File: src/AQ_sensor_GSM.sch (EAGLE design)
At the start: 83 parts, among them IC2 MCP73831/OT, J1 F-1X03-SIP-100-32, SW1 PCM12SMTR, U2 TEXAS_INSTRUMENTS_SN74HC125TE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, U3 TEXAS_INSTRUMENTS_LM1117IMP-3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, U4 ESP8266-12E/ESP-12E, U5 TP4056, U6 CP2102N-A02-GQFN28, U7 MT3608, X1 53048-08, X2 SIMLOCK-C707_10M006_512_2, X4 50 Ohms

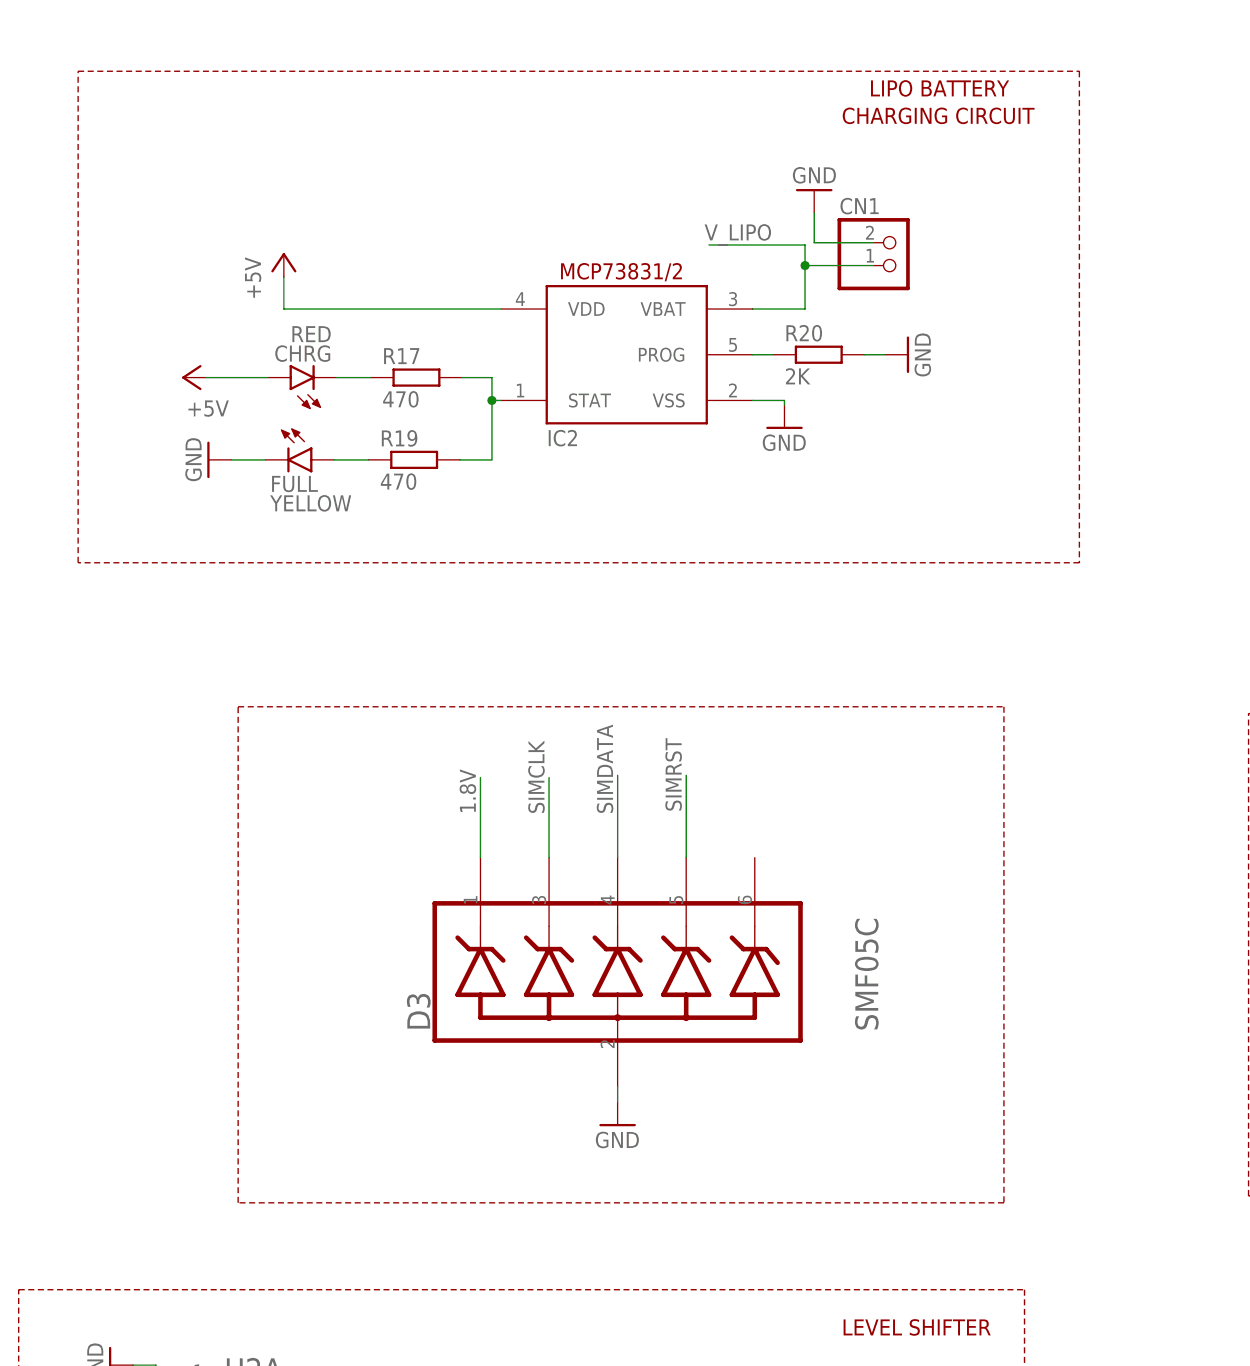
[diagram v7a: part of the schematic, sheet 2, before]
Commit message: Add GPS Module (L80-M39)
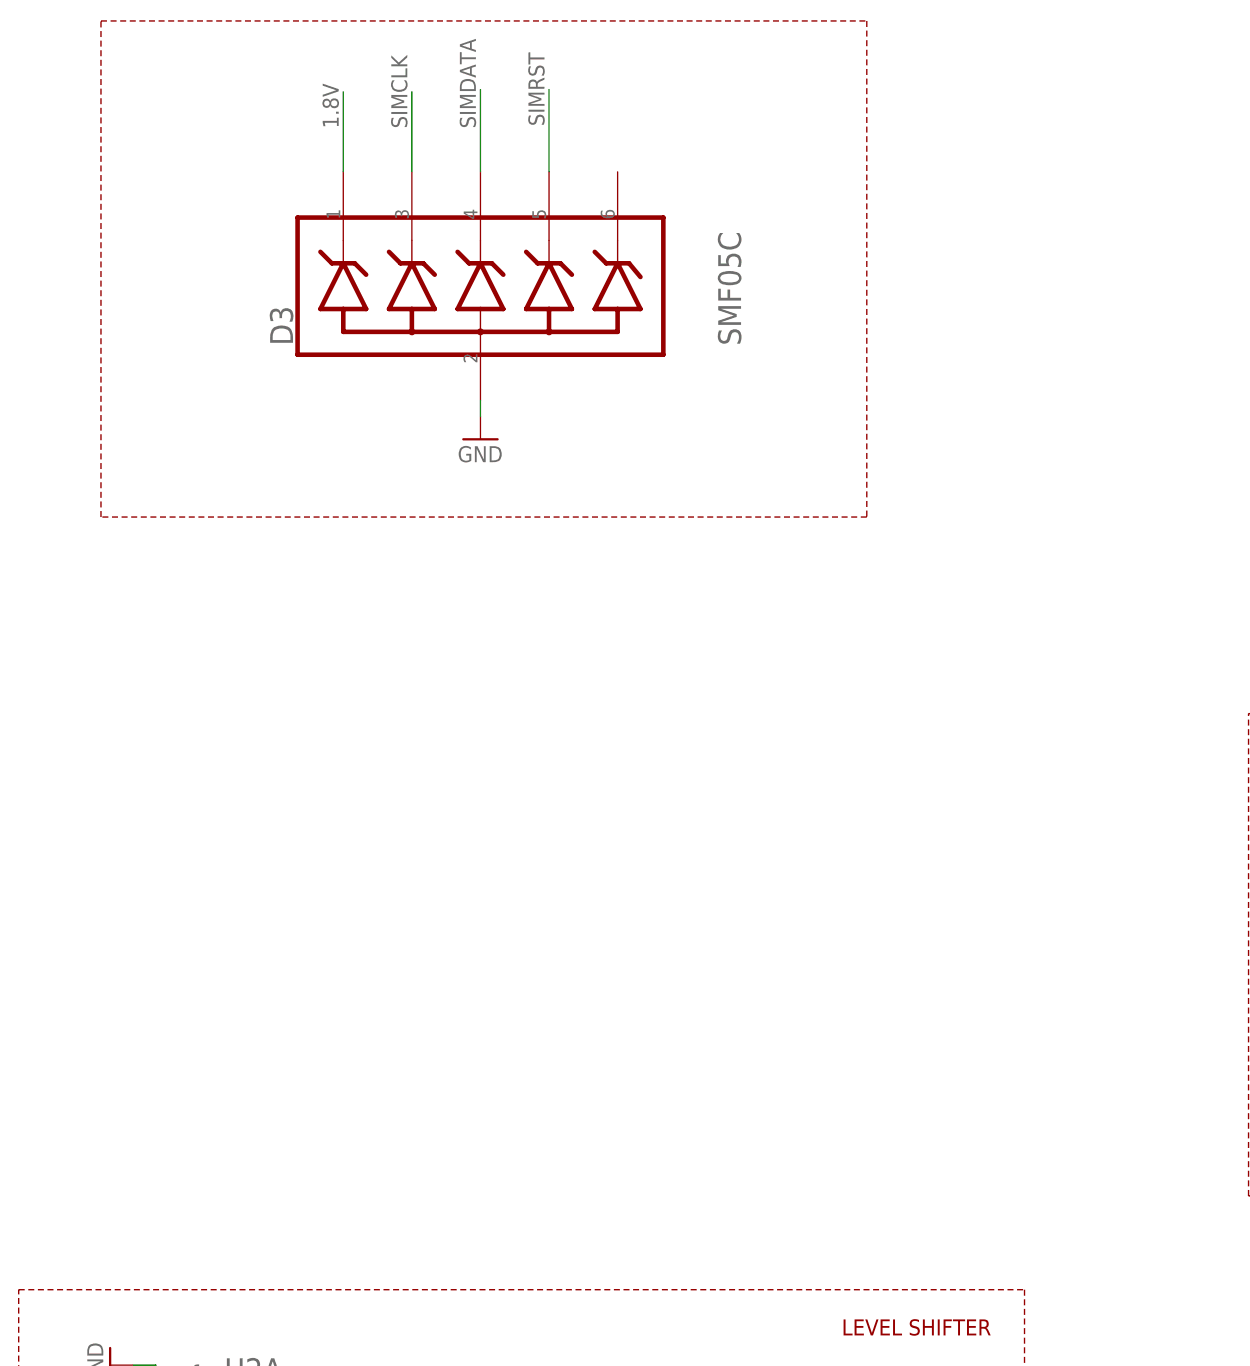
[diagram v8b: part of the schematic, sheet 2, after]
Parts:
- removed C2: TAJB106K016RNJ, Resistor_Capacitor:TAJB106K016RNJ
- removed CHRG: RED, led:LEDCHIP-LED0603
- removed CN1: (no value), AQ_sensor_GSM:JST_2PIN-SMT-RA
- removed FULL: YELLOW, led:LEDCHIP-LED0603
- removed IC2: MCP73831/OT, AQ_sensor_GSM:MCP73831/OT
- removed R17, R19: 470, rcl:R-EU_R0603
- removed R20: 2K, rcl:R-EU_R0603
- added U8: L80-M39, L80-M39:L80-M39
- C3: value TAJB106K016RNJ -> 100uF; device Resistor_Capacitor:TAJB106K016RNJ -> rcl:CPOL-EUD
- renumbered JP1 to EXPANSION
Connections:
- removed net N$12: FULL.A, R19.1
- removed net N$13: IC2.PROG, R20.1
- removed net N$6: CHRG.C, R17.1
- removed net N$9: IC2.STAT, R17.2, R19.2
- net +5V: no longer CHRG.A, EXPANSION.1, GPS.1, IC2.VDD, X1-8.S
- net 5V_REG: now also EXPANSION.1, GPS.1, X1-8.S
- net GND: now also C3.-; no longer C2.2, C3.2, CN1.1, FULL.C, IC2.VSS, R20.2
- net TP_VCC: now also C3.+; no longer C2.1
- net V_LIPO: no longer C3.1, CN1.2, IC2.VBAT
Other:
- note removed: "CHARGING CIRCUIT"
- note removed: "LIPO BATTERY"
- moved on the sheet: C1, C8, D3, U3
